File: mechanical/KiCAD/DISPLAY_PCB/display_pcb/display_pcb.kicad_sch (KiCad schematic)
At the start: 51 parts, among them J1 USB_C_Receptacle_USB2.0_16P, J2 Conn_01x18_Socket, J3 Conn_01x01_Pin, J4 Conn_01x01_Pin, J5 BTR, Q1 AO3401A, SW1 SW_MEC_5E, U1 ESP32-S3-WROOM-1, U3 USBLC6-2P6, U4 TP4056-42-ESOP8, U5 TLV75733PDBV, U6 ME6211C33M5

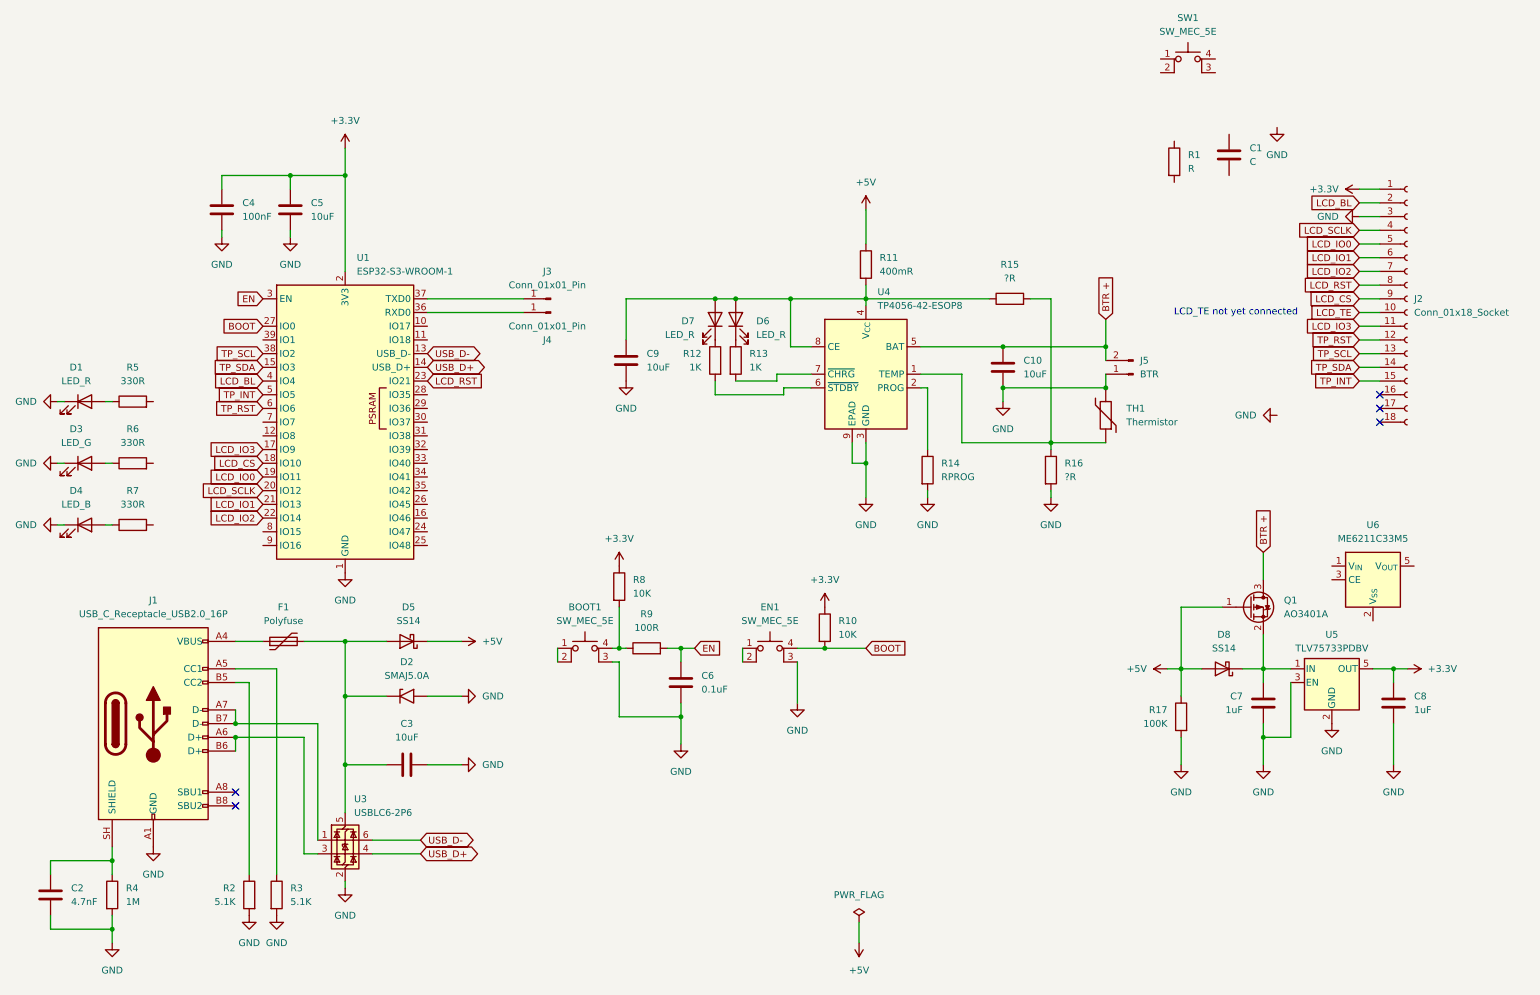
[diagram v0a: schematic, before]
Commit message: Small changes, missing battery protection IC, sorted the different related parts into groups
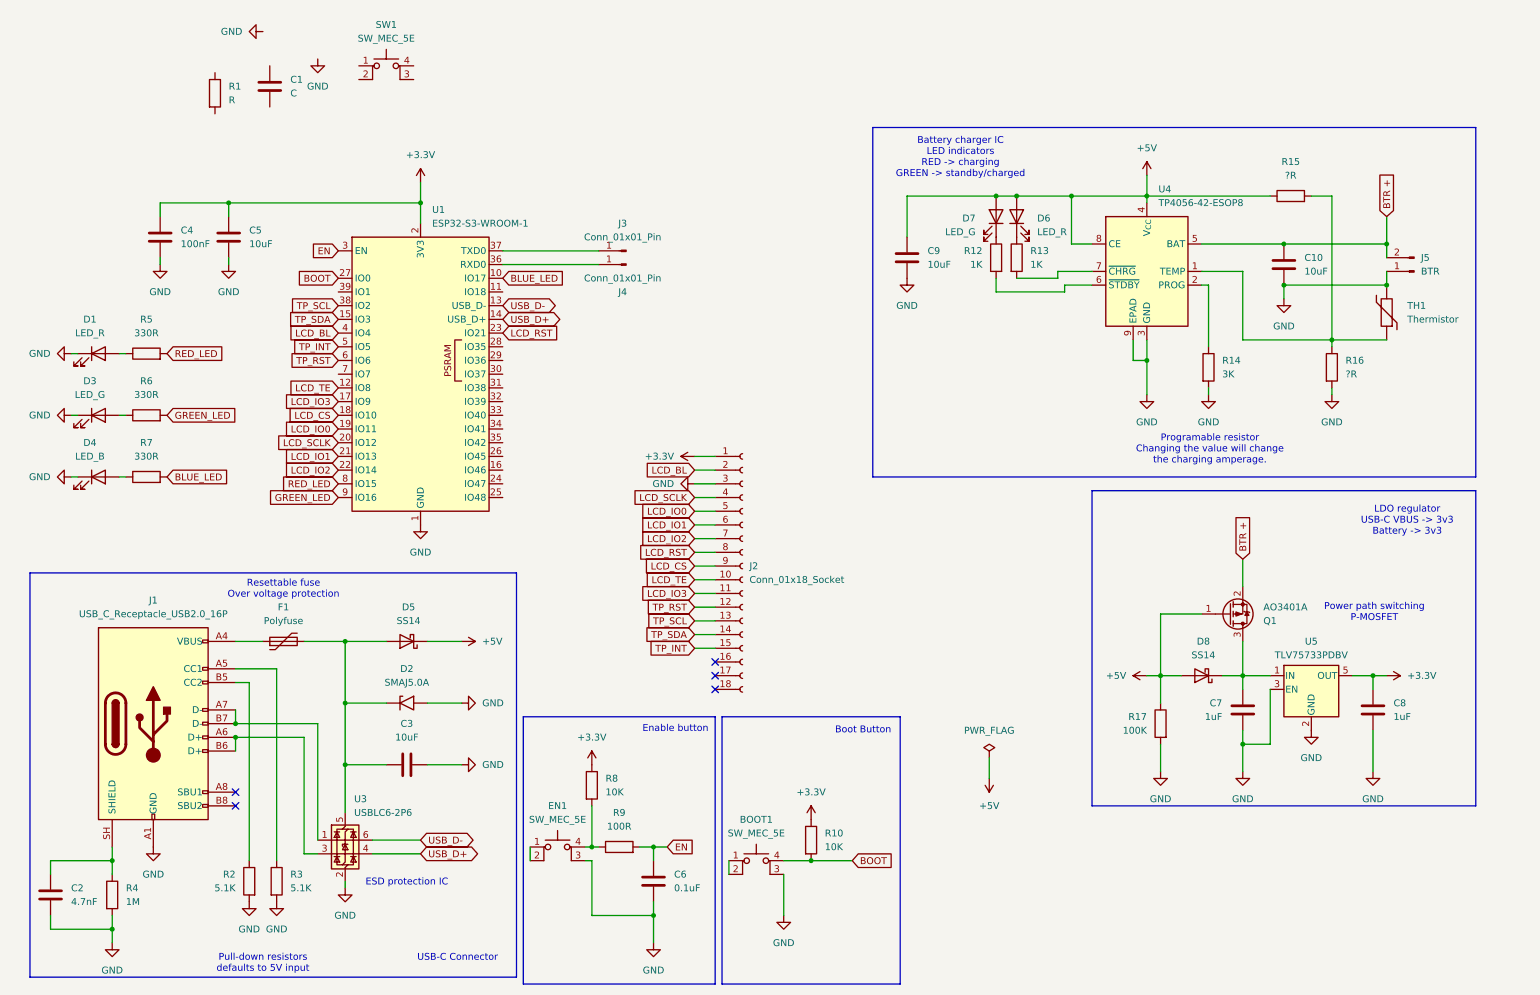
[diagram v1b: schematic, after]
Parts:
- removed R11: 400mR, symbol Device:R
- removed U6: ME6211C33M5, Package_TO_SOT_SMD:SOT-23-5, symbol Regulator_Linear:ME6211C33M5
- D7: value LED_R -> LED_G
- R14: value RPROG -> 3K
- renumbered EN1 to BOOT1, BOOT1 to EN1
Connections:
- net +5V: now also C9.1, D6.2 (A), D7.2 (A), R15.1, U4.4 (V_{CC}), U4.8 (CE)
- net BTR +: now also Q1.2 (S); no longer Q1.3 (D)
- net LCD_TE: now also U1.12 (IO8)
- net at C7.1, D8.1 (K), U5.1 (IN): now also Q1.3 (D); no longer Q1.2 (S)
- net GREEN_LED: now reaches R6.2
- net GREEN_LED: now also U1.9 (IO16)
- net BLUE_LED: now reaches U1.10 (IO17)
- net BLUE_LED: now also R7.2
- net RED_LED: now reaches U1.8 (IO15)
- net RED_LED: now also R5.2
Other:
- note added: "Battery charger IC LED indicators RED -> charging GREEN -> standby/charged"
- note added: "Boot Button"
- note added: "ESD protection IC"
- note added: "Enable button"
- note added: "LDO regulator USB-C VBUS -> 3v3 Battery -> 3v3"
- note added: "Power path switching P-MOSFET"
- note added: "Programable resistor Changing the value will change the charging amperage."
- note added: "Pull-down resistors defaults to 5V input"
- note added: "Resettable fuse Over voltage protection"
- note added: "USB-C Connector"
- note removed: "LCD_TE not yet connected"
- moved on the sheet: BOOT1, C1, C10, C4, C5, C6, C7, C8, C9, D1, D2, D3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

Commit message: Display schematic is finished, footprints are assigned, the basic board shape has been made, now the components has to be placed.
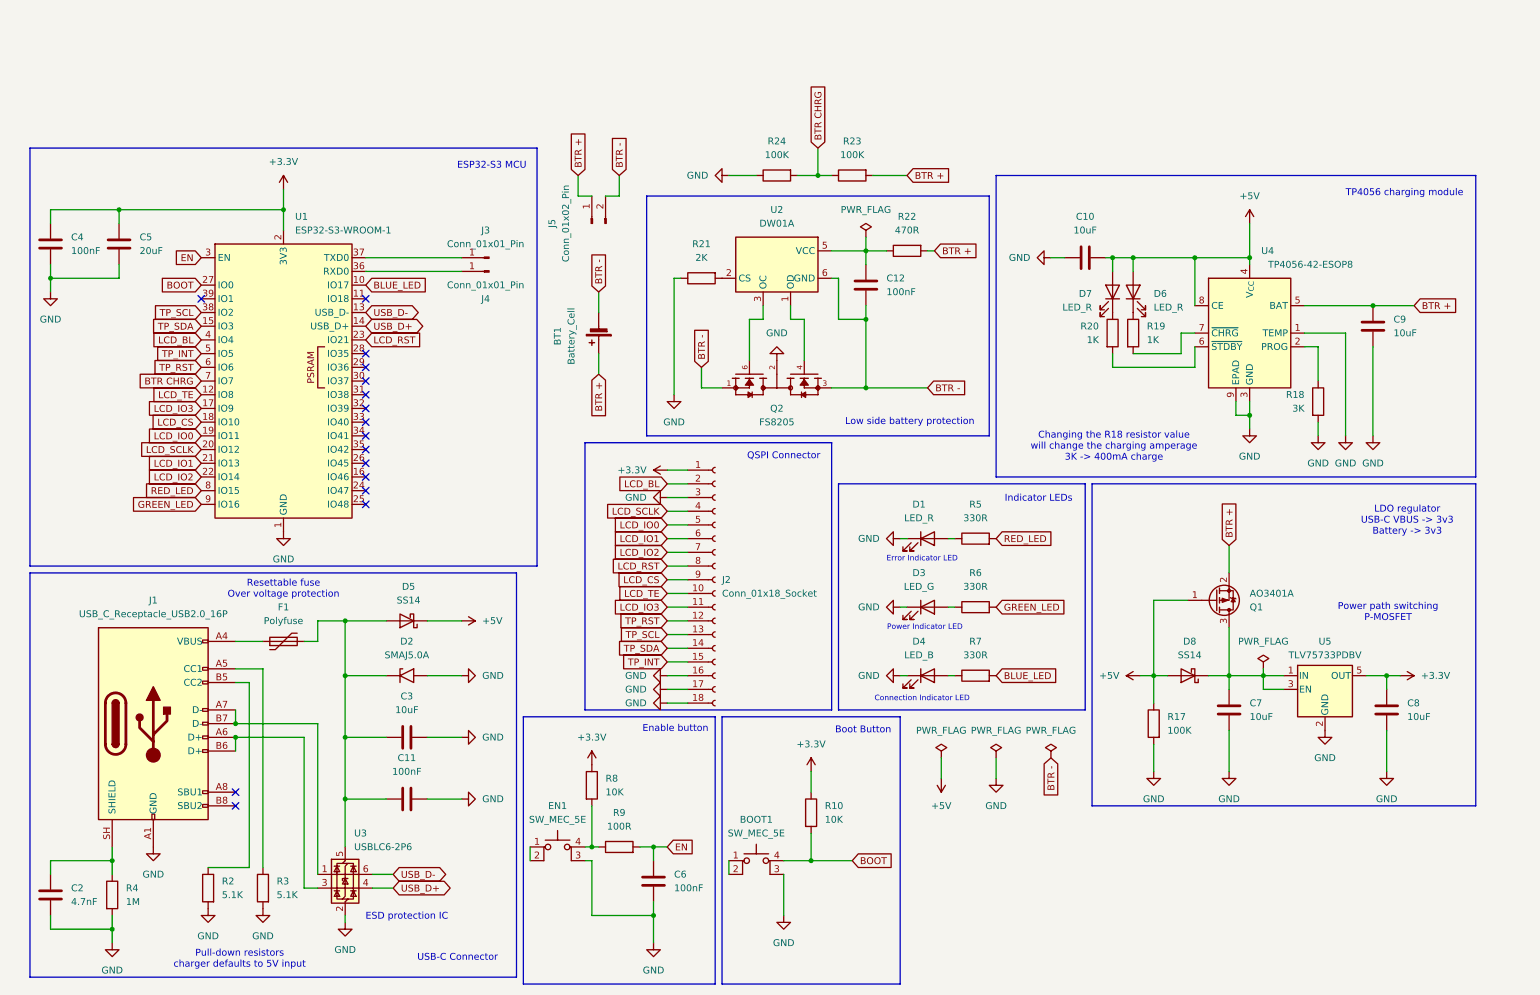
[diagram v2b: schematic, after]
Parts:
- removed C1: C, symbol Device:C
- removed R1: R, symbol Device:R
- removed R12, R13: 1K, symbol Device:R
- removed R14: 3K, symbol Device:R
- removed R15, R16: ?R, symbol Device:R
- removed SW1: SW_MEC_5E, Button_Switch_THT:SW_NKK_GW12LJP, symbol Switch:SW_MEC_5E
- removed TH1: Thermistor, symbol Device:Thermistor
- added BT1: Battery_Cell, symbol Device:Battery_Cell
- added C11, C12: 100nF, Capacitor_SMD:C_0805_2012Metric, symbol Device:C
- added Q2: FS8205, Package_SO:TSSOP-8_4.4x3mm_P0.65mm, symbol FS8205:FS8205
- added R18: 3K, Resistor_SMD:R_0805_2012Metric, symbol Device:R
- added R19, R20: 1K, Resistor_SMD:R_0805_2012Metric, symbol Device:R
- added R21: 2K, Resistor_SMD:R_0805_2012Metric, symbol Device:R
- added R22: 470R, Resistor_SMD:R_0805_2012Metric, symbol Device:R
- added R23, R24: 100K, Resistor_SMD:R_0805_2012Metric, symbol Device:R
- added U2: DW01A, Package_TO_SOT_SMD:SOT-23-6, symbol Battery_Management:DW01A
- BOOT1, EN1: footprint Button_Switch_THT:SW_NKK_GW12LJP -> Button_Switch_SMD:SW_SPST_EVQP2_MiddlePushTravel_H2.5mm
- C10, C3, C9: footprint (none) -> Capacitor_SMD:C_1206_3216Metric
- C2, C4: footprint (none) -> Capacitor_SMD:C_0805_2012Metric
- C5: value 10uF -> 20uF; footprint (none) -> Capacitor_SMD:C_1206_3216Metric
- C6: value 0.1uF -> 100nF; footprint (none) -> Capacitor_SMD:C_1206_3216Metric
- C7, C8: value 1uF -> 10uF; footprint (none) -> Capacitor_SMD:C_1206_3216Metric
- D1, D3, D4, D6: footprint (none) -> LED_SMD:LED_0805_2012Metric_Pad1.15x1.40mm_HandSolder
- D7: value LED_G -> LED_R; footprint (none) -> LED_SMD:LED_0805_2012Metric_Pad1.15x1.40mm_HandSolder
- J1: footprint Package_DFN_QFN:Texas_RNQ0040A_WQFN-40-1EP_6x4mm_P0.4mm_EP4.7x2.7mm -> Connector_USB:USB_C_Receptacle_GCT_USB4105-xx-A_16P_TopMnt_Horizontal
- J2: footprint Connector_FFC-FPC:TE_1-84952-8_1x18-1MP_P1.0mm_Horizontal -> Connector_FFC-FPC:Hirose_FH12-18S-0.5SH_1x18-1MP_P0.50mm_Horizontal
- J5: value BTR -> Conn_01x02_Pin; footprint Connector_PinHeader_1.27mm:PinHeader_1x02_P1.27mm_Vertical -> Connector_JST:JST_PH_S2B-PH-K_1x02_P2.00mm_Horizontal
- R10, R17, R2, R3, R5, R6, R7, R8, R9: footprint (none) -> Resistor_SMD:R_0805_2012Metric
- R4: footprint (none) -> Resistor_SMD:R_1206_3216Metric
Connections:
- net +5V: now also C10.2; no longer C9.1
- net BTR +: now also C9.1, J5.1 (Pin_1), BT1.1 (+), R22.2, R23.2; no longer C10.1, J5.2 (Pin_2)
- net GND: now also C10.1, J2.16 (Pin_16), J2.17 (Pin_17), J2.18 (Pin_18), U4.1 (TEMP), C11.1, Q2.2, Q2.5, R18.2, R21.1, R24.1; no longer C10.2, J5.1 (Pin_1), U5.3 (EN)
- net at C7.1, D8.1 (K), Q1.3 (D)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: now also U5.3 (EN)
- net at C3.2, D2.1 (A1), D5.2 (A)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: now also C11.2
- net at U4.2 (PROG): now also R18.1
- net BTR CHRG: now reaches U1.7 (IO7)
- net BTR CHRG: now also R23.1, R24.2
- net at D7.1 (K): now also R20.1
- net at U4.6 (~{STDBY}): now also R20.2
- net at D6.1 (K): now also R19.1
- net at U4.7 (~{CHRG}): now also R19.2
- new net: C12.1, R22.1, U2.5 (VCC)
- new net: Q2.4, U2.1 (OD)
- new net: R21.2, U2.2 (CS)
- new net: Q2.6, U2.3 (OC)
- new net BTR -: BT1.2 (-), C12.2, J5.2 (Pin_2), Q2.1, Q2.3, U2.6 (GND)
- no-connect marks 5 -> 16
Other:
- note added: "Changing the R18 resistor value will change the charging amperage 3K -> 400mA charge"
- note added: "Connection Indicator LED"
- note added: "ESP32-S3 MCU"
- note added: "Error Indicator LED"
- note added: "Indicator LEDs"
- note added: "Low side battery protection"
- note added: "Power Indicator LED"
- note added: "Pull-down resistors charger defaults to 5V input"
- note added: "QSPI Connector"
- note added: "TP4056 charging module"
- note removed: "Battery charger IC LED indicators RED -> charging GREEN -> standby/charged"
- note removed: "Programable resistor Changing the value will change the charging amperage."
- note removed: "Pull-down resistors defaults to 5V input"
- moved on the sheet: C3, C4, C5, C7, C8, D1, D2, D3, D4, D5, D8, J2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
